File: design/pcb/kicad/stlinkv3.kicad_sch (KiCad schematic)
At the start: 3 parts, among them U6 STLINK-V3MODS

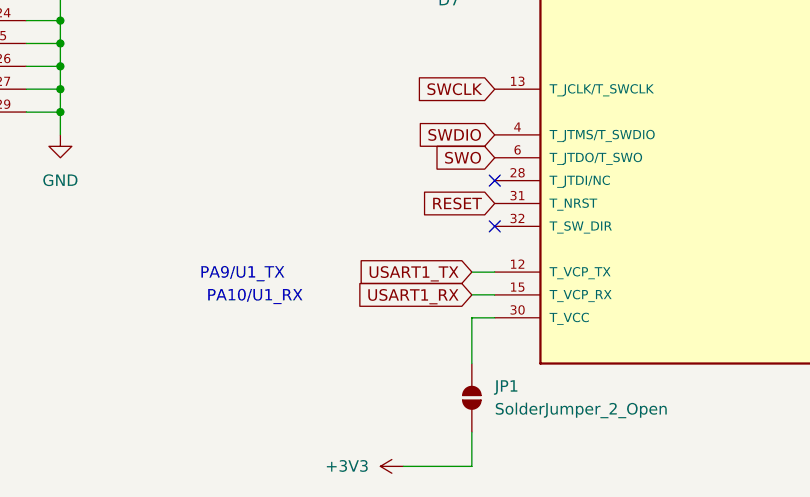
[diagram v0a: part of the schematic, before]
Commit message: Change of USB and STlink label
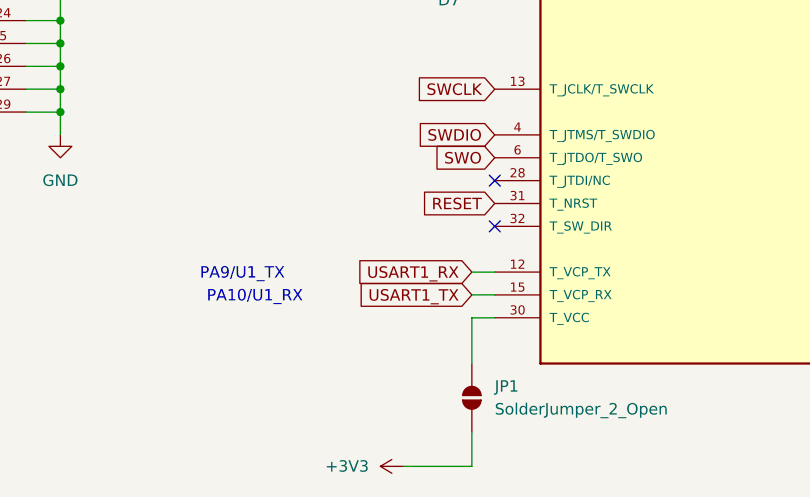
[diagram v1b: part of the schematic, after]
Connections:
- net USART1_RX: now also U6.12 (T_VCP_TX); no longer U6.15 (T_VCP_RX)
- net USART1_TX: now also U6.15 (T_VCP_RX); no longer U6.12 (T_VCP_TX)
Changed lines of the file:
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@@
+		)
+	)
+	(global_label "USART1_RX"
+		(shape input)
+		(at 144.78 109.22 180)
+		(fields_autoplaced yes)
+		(effects
+			(font
+				(size 1.27 1.27)
+			)
+			(justify right)
+		)
+		(property "Intersheetrefs" "${INTERSHEET_REFS}"
+			(at 131.272 109.22 0)
+			(effects
+				(font
+					(size 1.27 1.27)
+				)
+				(justify right)
+				(hide yes)
+			)
 		)
 	)
@@
 		)
 	)
-	(global_label "USART1_RX"
+	(global_label "USART1_TX"
 		(shape input)
 		(at 144.78 111.76 180)
@@
 		)
 		(property "Intersheetrefs" "${INTERSHEET_REFS}"
-			(at 131.272 111.76 0)
+			(at 131.5744 111.76 0)
 			(effects
 				(font
@@
 			(effects
 				(font
-					(size 1.27 1.27)
-				)
-				(justify right)
-				(hide yes)
-			)
-		)
-	)
-	(global_label "USART1_TX"
-		(shape input)
-		(at 144.78 109.22 180)
-		(fields_autoplaced yes)
-		(effects
-			(font
-				(size 1.27 1.27)
-			)
-			(justify right)
-		)
-		(property "Intersheetrefs" "${INTERSHEET_REFS}"
-			(at 131.5744 109.22 0)
-			(effects
-				(font
